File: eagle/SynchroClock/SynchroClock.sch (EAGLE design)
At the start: 39 parts, among them IC1 DS3231/SO, J1 VIN, U1 TC1262, U2 ATTINY85-P

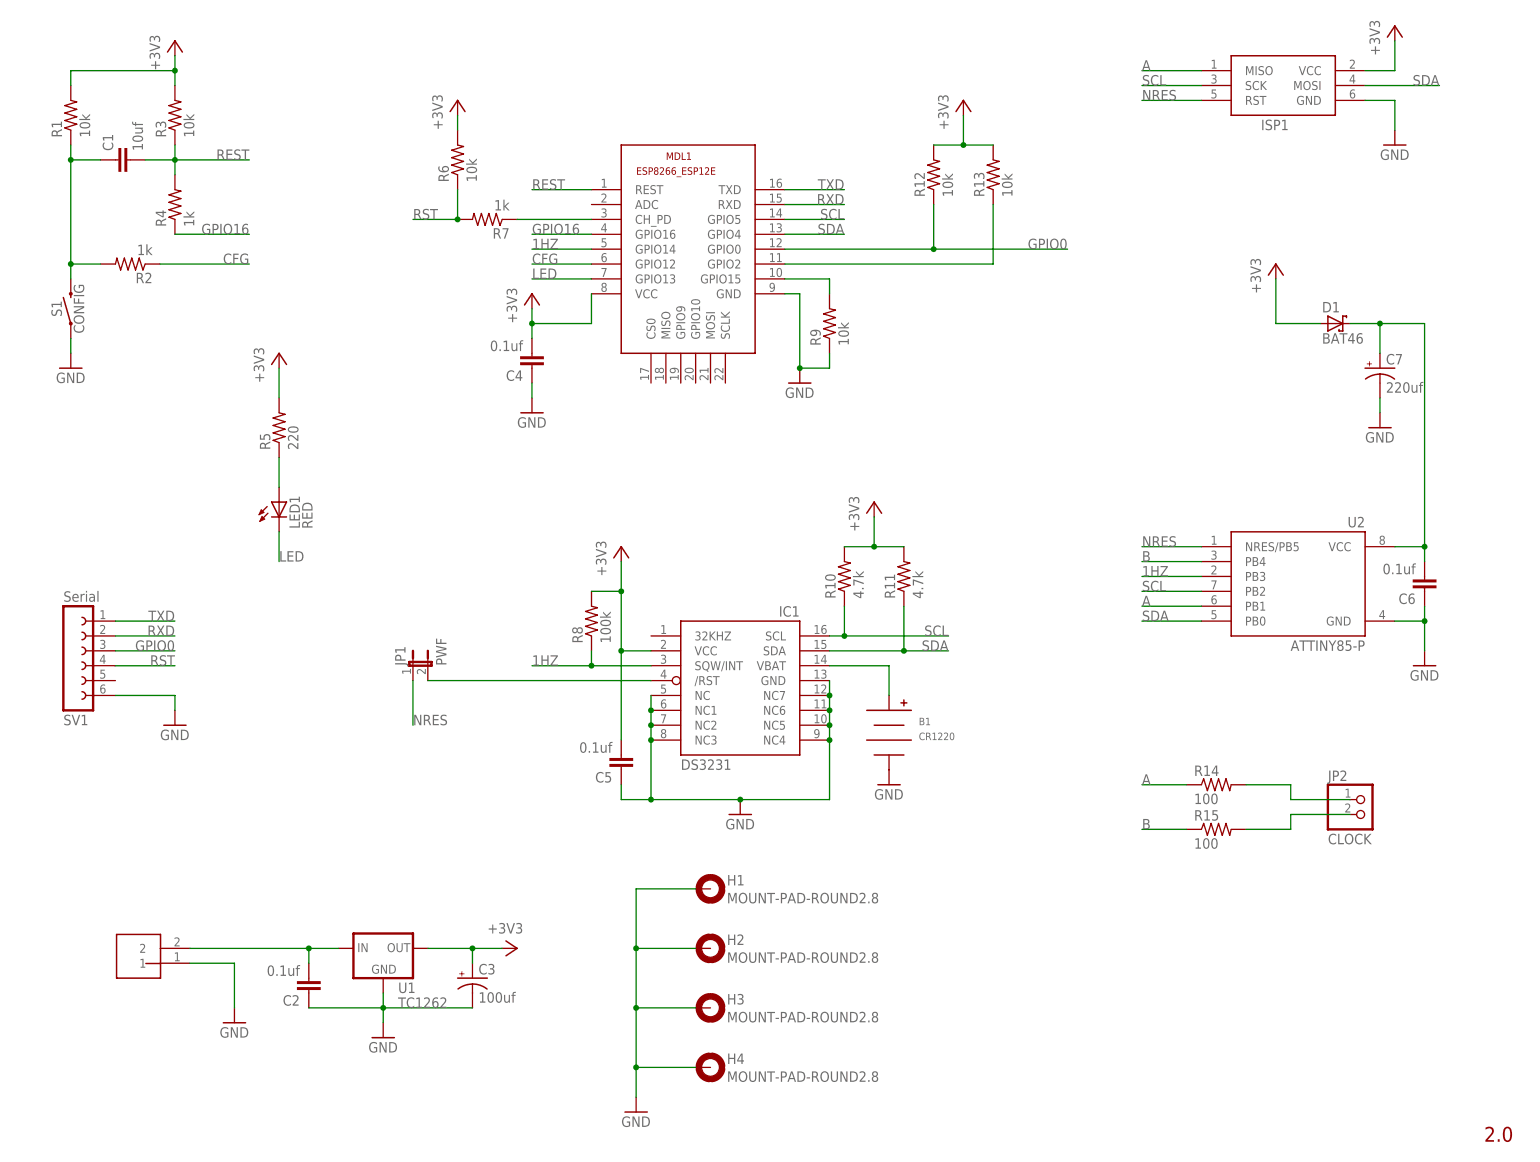
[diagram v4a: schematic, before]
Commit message: updated with new voltage regulator and pwrgd signal for power fail
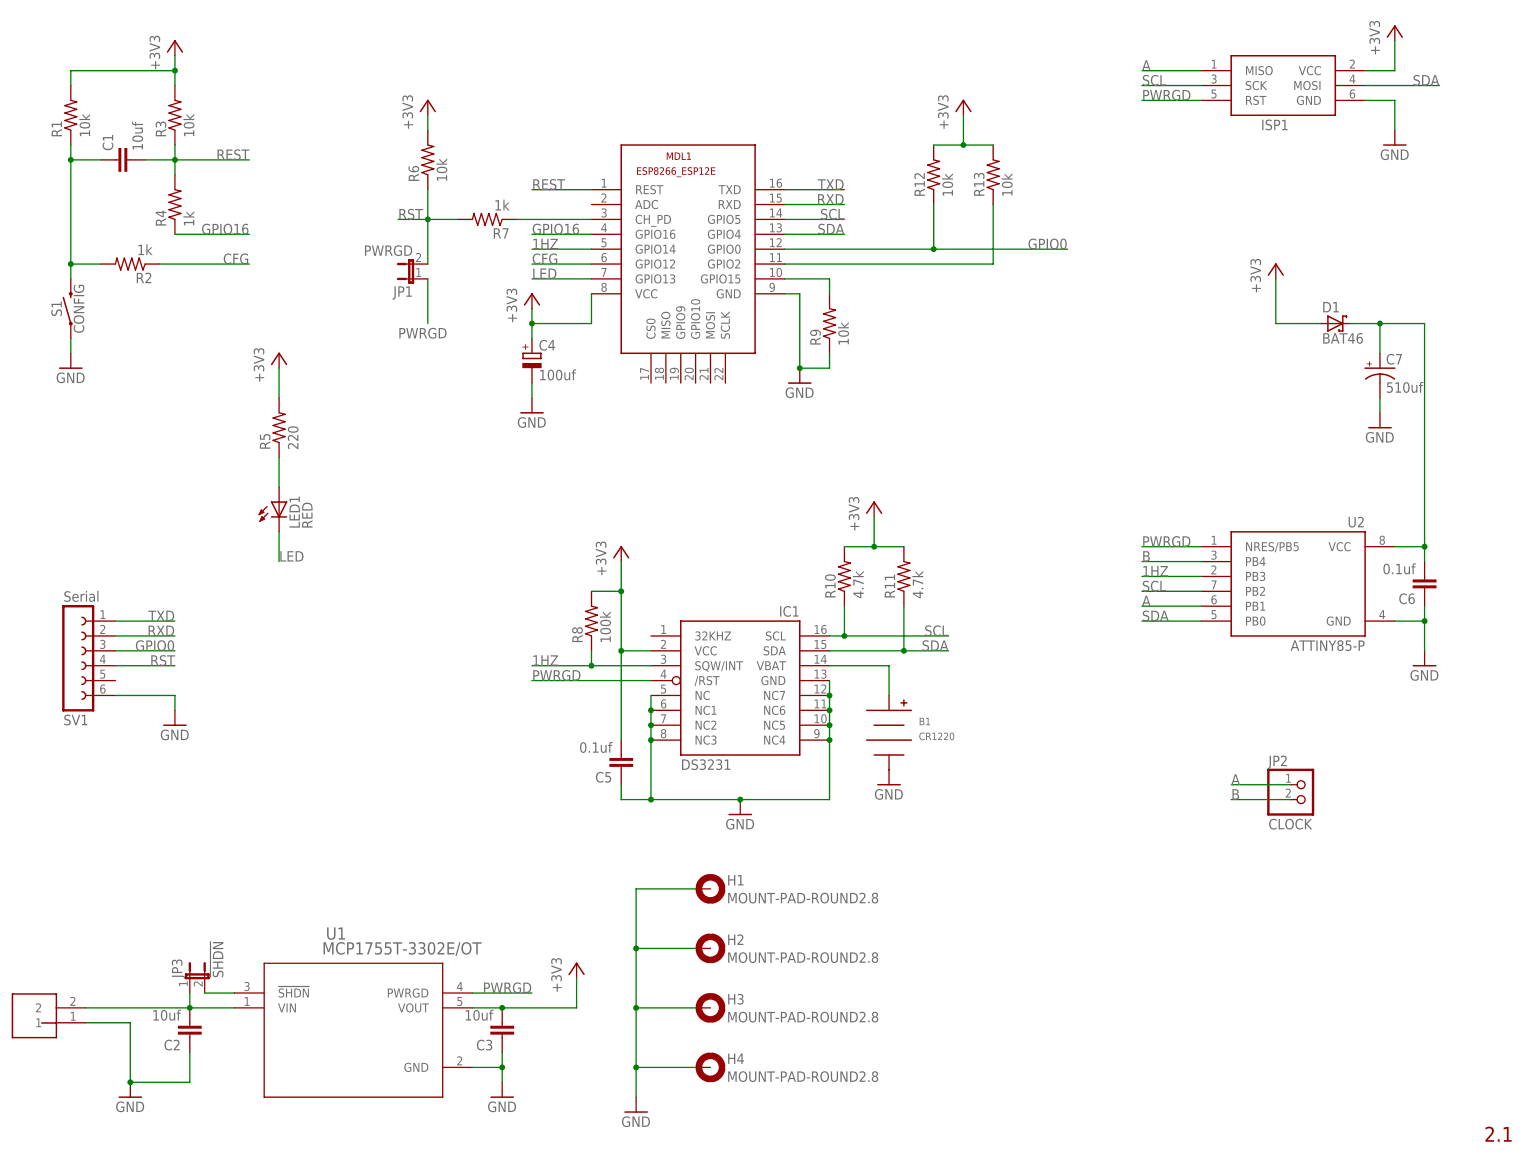
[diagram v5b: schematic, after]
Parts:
- removed R14, R15: 100, resistor:R-US_0204/2V
- added JP3: !SHDN, SynchroClock:JUMPER-2PTH
- C2: value 0.1uf -> 10uf; device capacitor-wima:C2.5/2 -> capacitor-wima:C5/2.5
- C3: value 100uf -> 10uf; device rcl:CPOL-USE2.5-5 -> capacitor-wima:C5/2.5
- C4: value 0.1uf -> 100uf; device capacitor-wima:C2.5/2 -> rcl:CPOL-EUE2.5-5
- C7: value 220uf -> 510uf; device rcl:CPOL-USE2.5-5 -> rcl:CPOL-USE3.5-8
- JP1: value PWF -> PWRGD
- U1: value TC1262 -> MCP1755T-3302E/OT; device SynchroClock:TC1262 -> SynchroClock:MCP1755T-3302E/OT
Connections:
- removed net N$11: JP2.2, R15.2
- removed net N$9: JP2.1, R14.2
- removed net NRES: ISP1.RST, JP1.1, U2.NRES/PB5
- removed net NRST: IC1./RST, JP1.2
- new net !SHDN: JP3.2, U1.!SHDN
- new net PWRGD: IC1./RST, ISP1.RST, JP1.1, U1.PWRGD, U2.NRES/PB5
- net +3V3: now also C3.2, C4.+, U1.VOUT; no longer C3.+, C4.2, U1.OUT
- net +5V: now also JP3.1, U1.VIN; no longer U1.IN
- net A: now also JP2.1; no longer R14.1
- net B: now also JP2.2; no longer R15.1
- net GND: now also C3.1, C4.-; no longer C3.-, C4.1
- net RST: now also JP1.2
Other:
- note added: "2.1"
- note removed: "2.0"
- moved on the sheet: C2, JP1, JP2, R6

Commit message: WIP
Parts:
- removed C6: 0.1uf, capacitor-wima:C2.5/2
- U1: value MCP1755T-3302E/OT -> MCP1825-33; device SynchroClock:MCP1755T-3302E/OT -> SynchroClock:MCP1825-3302E/AT
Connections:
- net !SHDN: now also U1.*SHDN; no longer U1.!SHDN
- net ATVCC: no longer C6.2
- net GND: no longer C6.1
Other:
- moved on the sheet: JP3, U1
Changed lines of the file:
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@@
 <part name="+3V34" library="supply1" library_urn="urn:adsk.eagle:library:371" deviceset="+3V3" device=""/>
 <part name="JP2" library="pinhead" library_urn="urn:adsk.eagle:library:325" deviceset="PINHD-1X2" device="" value="CLOCK"/>
-<part name="C6" library="capacitor-wima" library_urn="urn:adsk.eagle:library:116" deviceset="C" device="2.5/2" value="0.1uf"/>
 <part name="C5" library="capacitor-wima" library_urn="urn:adsk.eagle:library:116" deviceset="C" device="2.5/2" value="0.1uf"/>
 <part name="+3V35" library="supply1" library_urn="urn:adsk.eagle:library:371" deviceset="+3V3" device=""/>
@@
 <part name="+3V1" library="supply1" library_urn="urn:adsk.eagle:library:371" deviceset="+3V3" device=""/>
 <part name="GND12" library="supply1" library_urn="urn:adsk.eagle:library:371" deviceset="GND" device=""/>
-<part name="U1" library="SynchroClock" deviceset="MCP1755T-3302E/OT" device=""/>
 <part name="JP1" library="SynchroClock" deviceset="JUMPER-2" device="PTH" value="PWRGD"/>
 <part name="C3" library="capacitor-wima" library_urn="urn:adsk.eagle:library:116" deviceset="C" device="5/2.5" value="10uf"/>
 <part name="C4" library="rcl" library_urn="urn:adsk.eagle:library:334" deviceset="CPOL-EU" device="E2.5-5" package3d_urn="urn:adsk.eagle:package:23344/1" value="100uf"/>
 <part name="JP3" library="SynchroClock" deviceset="JUMPER-2" device="PTH" value="!SHDN"/>
+<part name="U1" library="SynchroClock" deviceset="MCP1825-3302E/AT" device="" value="MCP1825-33"/>
 </parts>
 <sheets>
@@
 <instance part="GND4" gate="1" x="96.52" y="15.24"/>
 <instance part="SV1" gate="G$1" x="22.86" y="91.44" rot="MR180"/>
-<instance part="GND3" gate="1" x="33.02" y="15.24"/>
+<instance part="GND3" gate="1" x="43.18" y="15.24"/>
 <instance part="+3V34" gate="G$1" x="109.22" y="38.1"/>
 <instance part="JP2" gate="G$1" x="233.68" y="66.04"/>
-<instance part="C6" gate="G$1" x="254" y="101.6" rot="R180"/>
 <instance part="C5" gate="G$1" x="116.84" y="71.12" rot="R180"/>
 <instance part="+3V35" gate="G$1" x="101.6" y="152.4"/>
@@
 <instance part="+3V1" gate="G$1" x="228.6" y="157.48"/>
 <instance part="GND12" gate="1" x="246.38" y="129.54"/>
-<instance part="U1" gate="A" x="48.26" y="33.02"/>
 <instance part="JP1" gate="A" x="81.28" y="154.94" rot="R90"/>
 <instance part="C3" gate="G$1" x="96.52" y="25.4" rot="R180"/>
 <instance part="C4" gate="G$1" x="101.6" y="142.24"/>
-<instance part="JP3" gate="A" x="43.18" y="35.56"/>
+<instance part="JP3" gate="A" x="43.18" y="38.1"/>
+<instance part="U1" gate="A" x="68.58" y="33.02"/>
 </instances>
 <busses>
@@
 </segment>
 <segment>
-<pinref part="U1" gate="A" pin="VOUT"/>
-<wire x1="91.44" y1="30.48" x2="96.52" y2="30.48" width="0.1524" layer="91"/>
 <pinref part="+3V34" gate="G$1" pin="+3V3"/>
 <wire x1="96.52" y1="30.48" x2="109.22" y2="30.48" width="0.1524" layer="91"/>
 <wire x1="109.22" y1="30.48" x2="109.22" y2="35.56" width="0.1524" layer="91"/>
 <pinref part="C3" gate="G$1" pin="2"/>
+<pinref part="U1" gate="A" pin="VOUT"/>
+<wire x1="86.36" y1="30.48" x2="96.52" y2="30.48" width="0.1524" layer="91"/>
 <junction x="96.52" y="30.48"/>
 </segment>
@@
 <net name="PWRGD" class="0">
 <segment>
-<pinref part="U1" gate="A" pin="PWRGD"/>
-<wire x1="91.44" y1="33.02" x2="101.6" y2="33.02" width="0.1524" layer="91"/>
-<label x="101.6" y="33.02" size="1.778" layer="95" rot="MR0"/>
-</segment>
-<segment>
 <pinref part="IC1" gate="G$1" pin="/RST"/>
 <wire x1="121.92" y1="86.36" x2="101.6" y2="86.36" width="0.1524" layer="91"/>
@@
 <wire x1="83.82" y1="154.94" x2="83.82" y2="147.32" width="0.1524" layer="91"/>
 <label x="78.74" y="144.78" size="1.778" layer="95"/>
+</segment>
+<segment>
+<pinref part="U1" gate="A" pin="PWRGD"/>
+<wire x1="86.36" y1="35.56" x2="96.52" y2="35.56" width="0.1524" layer="91"/>
+<label x="96.52" y="35.56" size="1.778" layer="95" rot="MR0"/>
 </segment>
 </net>
@@
 </segment>
 <segment>
-<pinref part="GND3" gate="1" pin="GND"/>
-<wire x1="33.02" y1="27.94" x2="33.02" y2="17.78" width="0.1524" layer="91"/>
-<wire x1="25.4" y1="27.94" x2="33.02" y2="27.94" width="0.1524" layer="91"/>
-<pinref part="J1" gate="J$1" pin="1"/>
-<pinref part="C2" gate="G$1" pin="1"/>
-<wire x1="43.18" y1="22.86" x2="43.18" y2="17.78" width="0.1524" layer="91"/>
-<wire x1="43.18" y1="17.78" x2="33.02" y2="17.78" width="0.1524" layer="91"/>
-<junction x="33.02" y="17.78"/>
-</segment>
-<segment>
 <pinref part="GND5" gate="1" pin="GND"/>
 <wire x1="101.6" y1="137.16" x2="101.6" y2="134.62" width="0.1524" layer="91"/>
@@
 <pinref part="U2" gate="G$1" pin="GND"/>
 <wire x1="248.92" y1="96.52" x2="254" y2="96.52" width="0.1524" layer="91"/>
-<pinref part="C6" gate="G$1" pin="1"/>
-<wire x1="254" y1="96.52" x2="254" y2="99.06" width="0.1524" layer="91"/>
 <pinref part="GND11" gate="1" pin="GND"/>
 <wire x1="254" y1="96.52" x2="254" y2="91.44" width="0.1524" layer="91"/>
-<junction x="254" y="96.52"/>
 </segment>
 <segment>
@@
 <segment>
 <pinref part="GND4" gate="1" pin="GND"/>
-<wire x1="96.52" y1="22.86" x2="96.52" y2="20.32" width="0.1524" layer="91"/>
+<wire x1="96.52" y1="22.86" x2="96.52" y2="17.78" width="0.1524" layer="91"/>
+<pinref part="C3" gate="G$1" pin="1"/>
+</segment>
+<segment>
+<pinref part="J1" gate="J$1" pin="1"/>
+<wire x1="25.4" y1="27.94" x2="33.02" y2="27.94" width="0.1524" layer="91"/>
+<wire x1="33.02" y1="27.94" x2="33.02" y2="17.78" width="0.1524" layer="91"/>
+<pinref part="GND3" gate="1" pin="GND"/>
+<wire x1="33.02" y1="17.78" x2="43.18" y2="17.78" width="0.1524" layer="91"/>
+<pinref part="C2" gate="G$1" pin="1"/>
+<wire x1="43.18" y1="17.78" x2="43.18" y2="22.86" width="0.1524" layer="91"/>
+<junction x="43.18" y="17.78"/>
+<wire x1="43.18" y1="17.78" x2="48.26" y2="17.78" width="0.1524" layer="91"/>
+<wire x1="48.26" y1="17.78" x2="48.26" y2="25.4" width="0.1524" layer="91"/>
 <pinref part="U1" gate="A" pin="GND"/>
-<wire x1="96.52" y1="20.32" x2="96.52" y2="17.78" width="0.1524" layer="91"/>
-<wire x1="91.44" y1="20.32" x2="96.52" y2="20.32" width="0.1524" layer="91"/>
-<junction x="96.52" y="20.32"/>
-<pinref part="C3" gate="G$1" pin="1"/>
+<wire x1="48.26" y1="25.4" x2="50.8" y2="25.4" width="0.1524" layer="91"/>
 </segment>
 </net>
@@
 <wire x1="246.38" y1="142.24" x2="246.38" y2="147.32" width="0.1524" layer="91"/>
 <junction x="246.38" y="147.32"/>
-<pinref part="C6" gate="G$1" pin="2"/>
 <pinref part="U2" gate="G$1" pin="VCC"/>
-<wire x1="254" y1="109.22" x2="254" y2="106.68" width="0.1524" layer="91"/>
 <wire x1="248.92" y1="109.22" x2="254" y2="109.22" width="0.1524" layer="91"/>
 <wire x1="254" y1="147.32" x2="254" y2="109.22" width="0.1524" layer="91"/>
-<junction x="254" y="109.22"/>
 </segment>
 </net>
@@
 <pinref part="C2" gate="G$1" pin="2"/>
 <wire x1="25.4" y1="30.48" x2="43.18" y2="30.48" width="0.1524" layer="91"/>
-<pinref part="U1" gate="A" pin="VIN"/>
 <wire x1="43.18" y1="30.48" x2="50.8" y2="30.48" width="0.1524" layer="91"/>
 <junction x="43.18" y="30.48"/>
 <pinref part="JP3" gate="A" pin="1"/>
-<wire x1="43.18" y1="33.02" x2="43.18" y2="30.48" width="0.1524" layer="91"/>
+<wire x1="43.18" y1="35.56" x2="43.18" y2="30.48" width="0.1524" layer="91"/>
+<pinref part="U1" gate="A" pin="VIN"/>
 </segment>
 </net>
@@
 </segment>
 </net>
-<net name="!SHDN" class="1">
-<segment>
-<pinref part="U1" gate="A" pin="!SHDN"/>
+<net name="!SHDN" class="0">
+<segment>
 <pinref part="JP3" gate="A" pin="2"/>
-<wire x1="50.8" y1="33.02" x2="45.72" y2="33.02" width="0.1524" layer="91"/>
-</segment>
-</net>
+<pinref part="U1" gate="A" pin="*SHDN"/>
+<wire x1="45.72" y1="35.56" x2="50.8" y2="35.56" width="0.1524" layer="91"/>
+</segment>
+</net>

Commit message: board version 2.1
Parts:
- removed ISP1: AVRISP-6, SynchroClock:AVRISP-6
- JP1: value PWRGD -> !SHDN
- JP2: value CLOCK -> PWRGD; device pinhead:PINHD-1X2 -> SynchroClock:JUMPER-2PTH
- JP3: value !SHDN -> CLOCK; device SynchroClock:JUMPER-2PTH -> pinhead:PINHD-1X2
- renumbered C7 to C6
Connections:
- net !SHDN: now also JP1.2; no longer JP3.2
- net +3V3: no longer ISP1.VCC
- net +5V: now also JP1.1; no longer JP3.1
- net A: now also JP3.1; no longer ISP1.MISO, JP2.1
- net B: now also JP3.2; no longer JP2.2
- net GND: no longer ISP1.GND
- net PWRGD: now also JP2.1; no longer ISP1.RST, JP1.1
- net RST: now also JP2.2; no longer JP1.2
- net SCL: no longer ISP1.SCK
- net SDA: no longer ISP1.MOSI
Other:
- moved on the sheet: JP1
